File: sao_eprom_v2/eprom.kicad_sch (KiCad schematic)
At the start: 7 parts, among them U4 74LS573, U7 74LS573

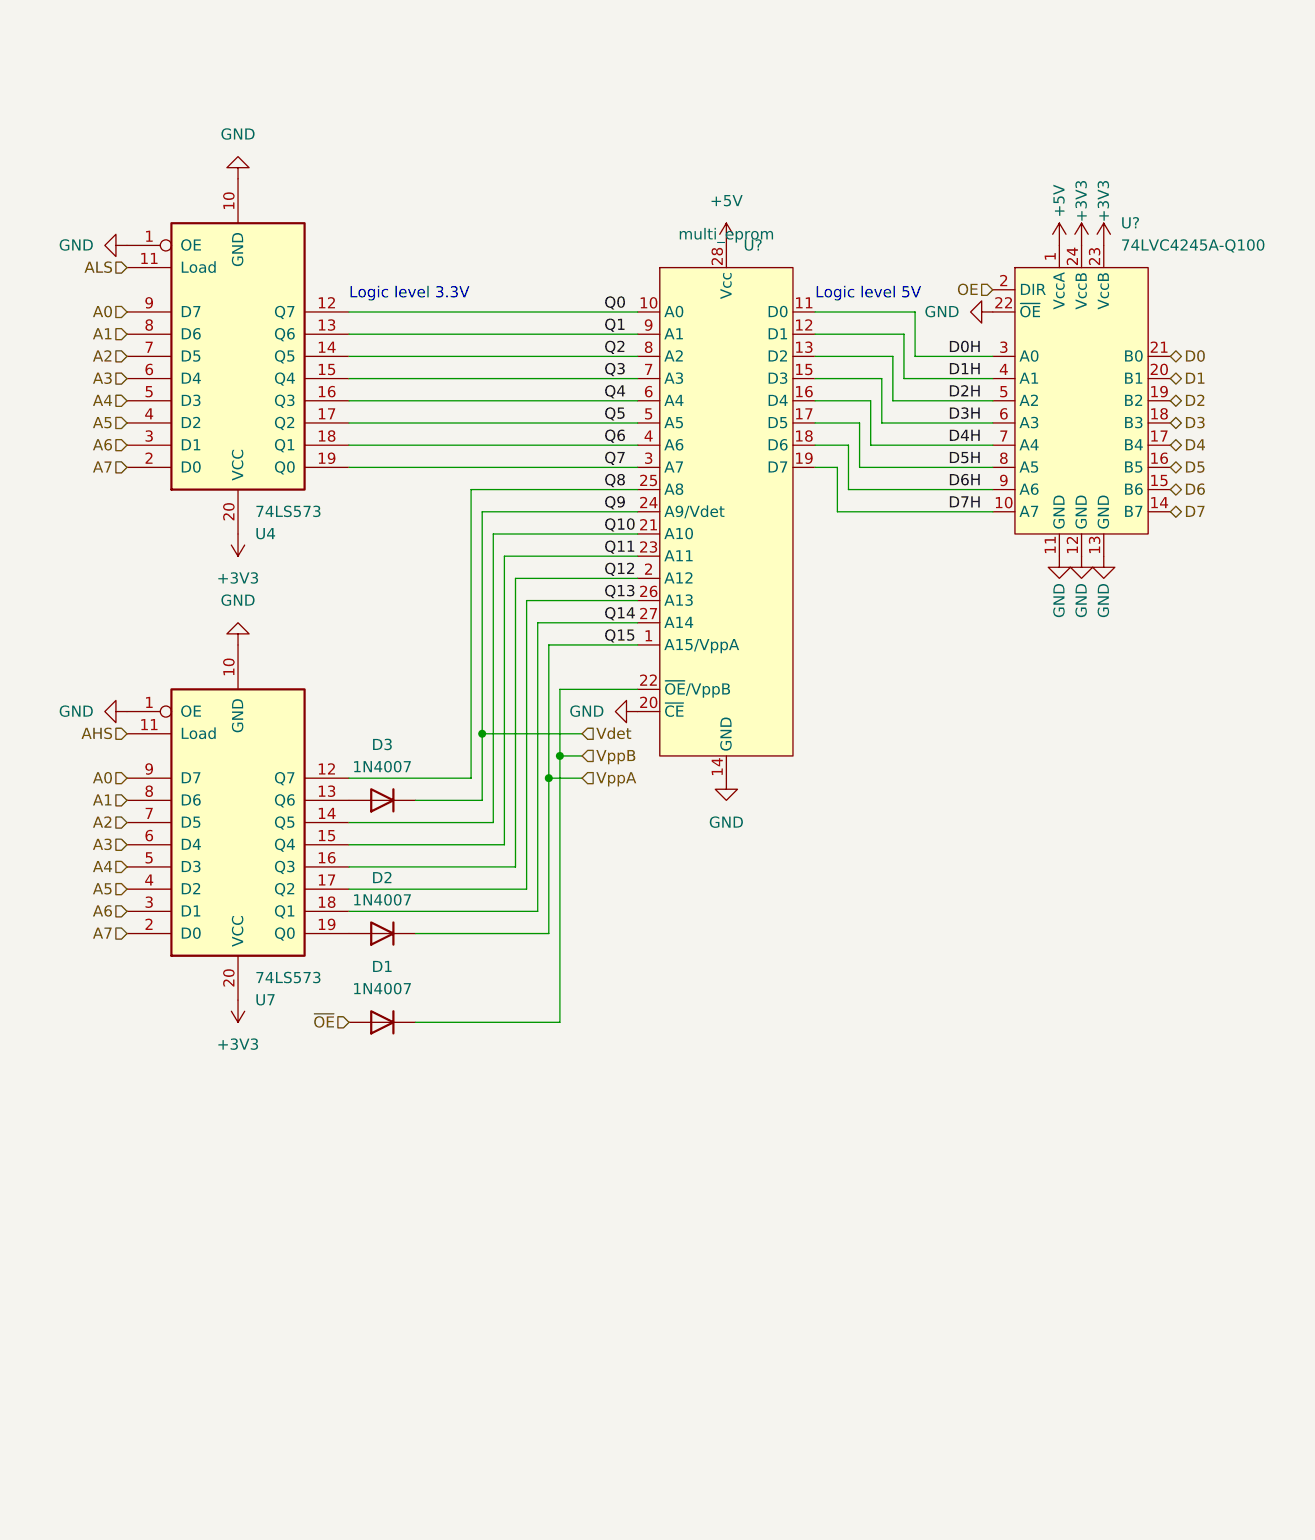
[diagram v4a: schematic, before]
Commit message: Add some blinkenlights!
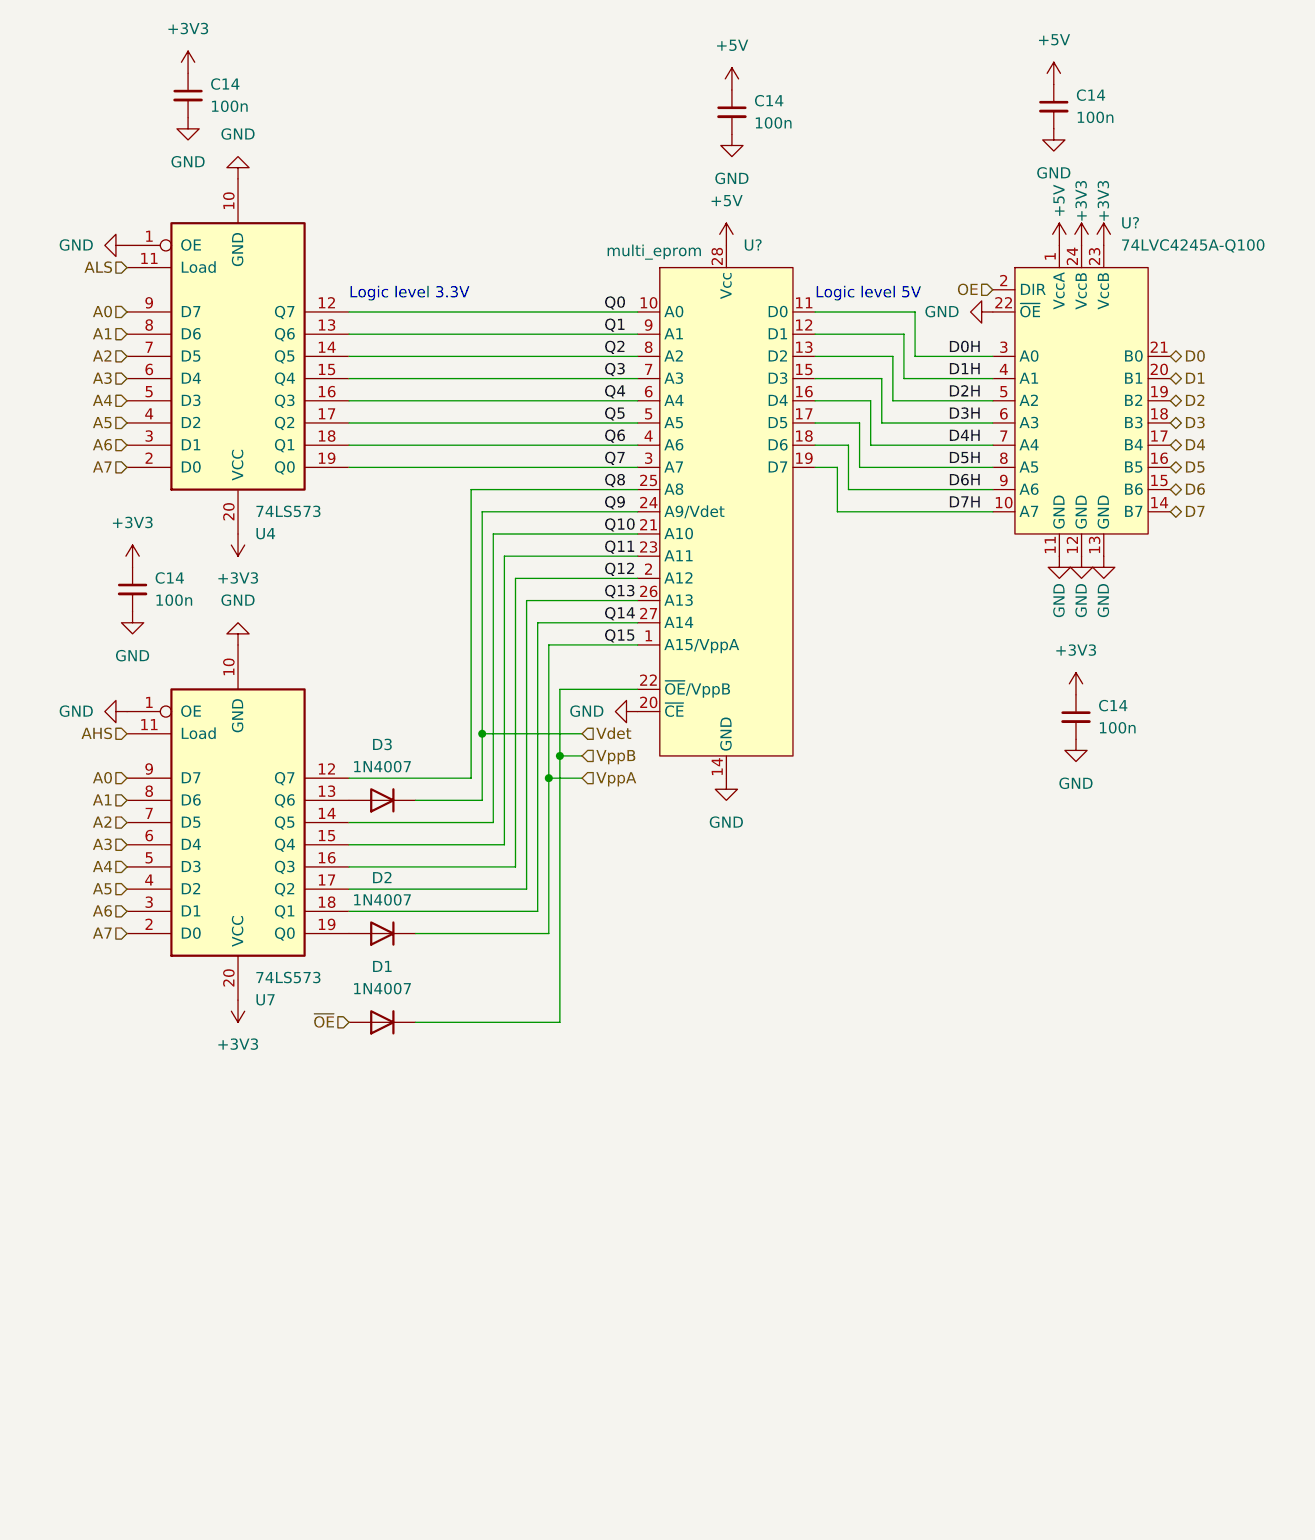
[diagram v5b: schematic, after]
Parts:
- added C14 (x5): 100n, Capacitor_SMD:C_0402_1005Metric_Pad0.74x0.62mm_HandSolder, symbol Device:C_Small
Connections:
- net +3V3: now also C14.1, C14.1, C14.1
- net +5V: now also C14.1, C14.1
- net GND: now also C14.2, C14.2, C14.2, C14.2, C14.2

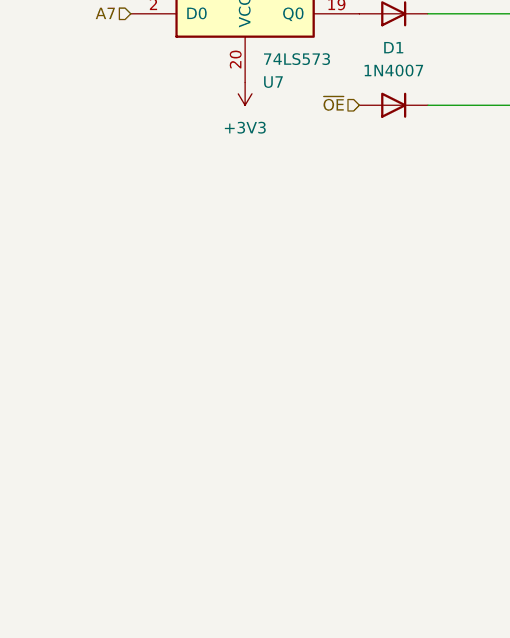
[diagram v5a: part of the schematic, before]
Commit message: Now with QWIIC and TestPads!
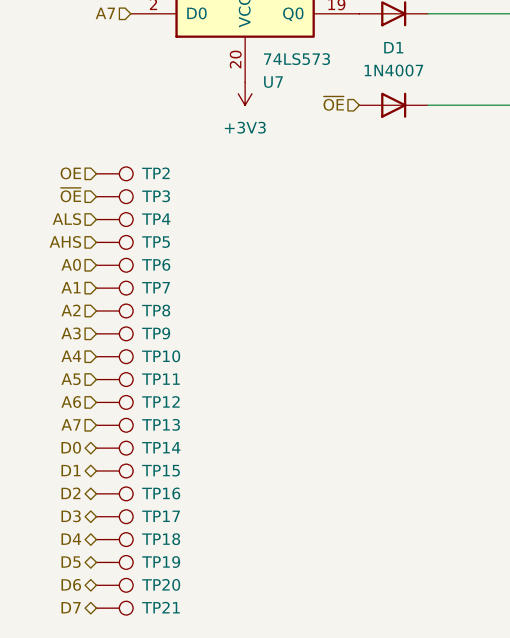
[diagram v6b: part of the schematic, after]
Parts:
- added TP10, TP11, TP12, TP13, TP14, TP15, TP16, TP17, TP18, TP19, TP2, TP20, TP21, TP3, TP4, TP5, TP6, TP7, TP8, TP9: TestPoint, TestPoint:TestPoint_Pad_D1.0mm, symbol Connector:TestPoint
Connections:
- net A0: now also TP6.1
- net A1: now also TP7.1
- net A2: now also TP8.1
- net A3: now also TP9.1
- net A4: now also TP10.1
- net A5: now also TP11.1
- net A6: now also TP12.1
- net A7: now also TP13.1
- net AHS: now also TP5.1
- net ALS: now also TP4.1
- net D0: now also TP14.1
- net D1: now also TP15.1
- net D2: now also TP16.1
- net D3: now also TP17.1
- net D4: now also TP18.1
- net D5: now also TP19.1
- net D6: now also TP20.1
- net D7: now also TP21.1
- net OE: now also TP2.1
- net ~{OE}: now also TP3.1

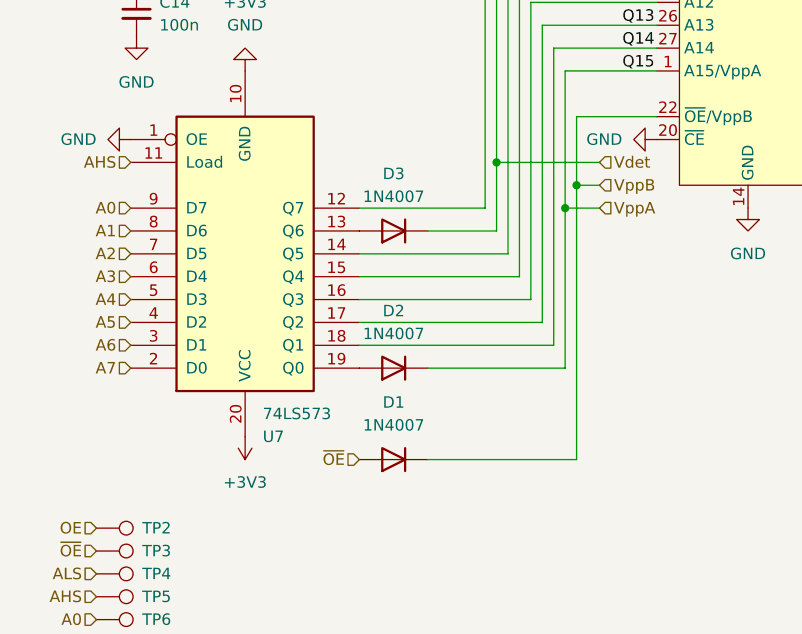
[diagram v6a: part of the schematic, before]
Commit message: Put yet another feedback in my design
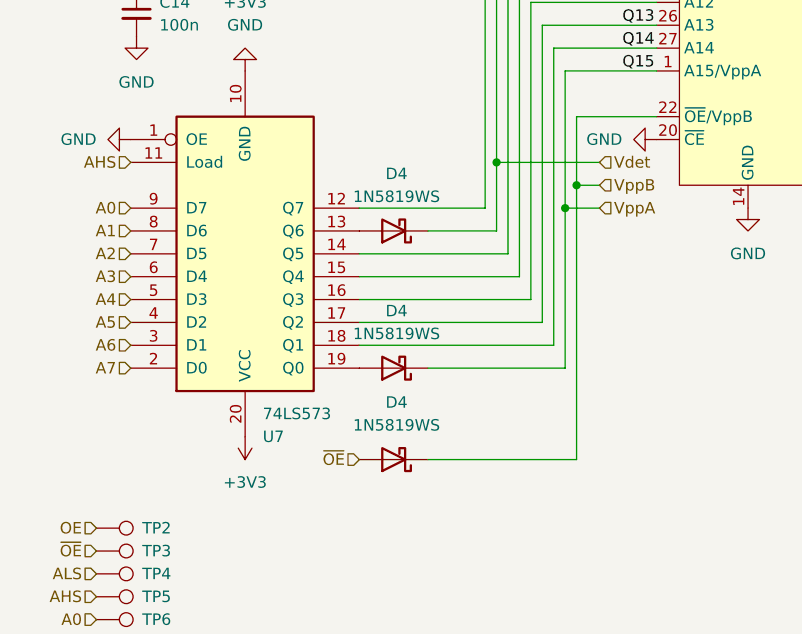
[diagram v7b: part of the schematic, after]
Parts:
- removed D1, D2, D3: 1N4007, Diode_SMD:D_SOD-123F, symbol Diode:1N4007
- added D4 (x3): 1N5819WS, Diode_SMD:D_SOD-323_HandSoldering, symbol Diode:1N5819WS
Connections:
- net Vdet: now also D4.1 (K)
- net VppA: now also D4.1 (K)
- net VppB: now also D4.1 (K)
- net ~{OE}: now also D4.2 (A)
- net at U7.13 (Q6): now also D4.2 (A)
- net at U7.19 (Q0): now also D4.2 (A)
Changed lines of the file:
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@@
-    )
-  )
-  (symbol (lib_id "Diode:1N4007") (at 87.63 101.6 180) (unit 1)
-    (in_bom yes) (on_board yes) (dnp no) (fields_autoplaced)
-    (property "Reference" "D3" (at 87.63 95.25 0)
-      (effects (font (size 1.27 1.27)))
-    )
-    (property "Value" "1N4007" (at 87.63 97.79 0)
-      (effects (font (size 1.27 1.27)))
-    )
-    (property "Footprint" "Diode_SMD:D_SOD-123F" (at 87.63 97.155 0)
-      (effects (font (size 1.27 1.27)) hide)
-    )
-    (property "Datasheet" "http://www.vishay.com/docs/88503/1n4001.pdf" (at 87.63 101.6 0)
-      (effects (font (size 1.27 1.27)) hide)
-    )
-    (property "Sim.Device" "D" (at 87.63 101.6 0)
-      (effects (font (size 1.27 1.27)) hide)
-    )
-    (property "Sim.Pins" "1=K 2=A" (at 87.63 101.6 0)
-      (effects (font (size 1.27 1.27)) hide)
-    )
-    (pin "1")
-    (pin "2")
-    (instances
-      (project "sao_eprom_v2"
-        (path "/07beccdd-32b3-4f03-aa51-fb5544b6f2d4/1053addf-4f12-44cd-9743-7d35ca2d08ac"
-          (reference "D3") (unit 1)
-        )
-      )
     )
   )
@@
     )
   )
-  (symbol (lib_id "Diode:1N4007") (at 87.63 127 180) (unit 1)
-    (in_bom yes) (on_board yes) (dnp no) (fields_autoplaced)
-    (property "Reference" "D1" (at 87.63 120.65 0)
-      (effects (font (size 1.27 1.27)))
-    )
-    (property "Value" "1N4007" (at 87.63 123.19 0)
-      (effects (font (size 1.27 1.27)))
-    )
-    (property "Footprint" "Diode_SMD:D_SOD-123F" (at 87.63 122.555 0)
-      (effects (font (size 1.27 1.27)) hide)
-    )
-    (property "Datasheet" "http://www.vishay.com/docs/88503/1n4001.pdf" (at 87.63 127 0)
-      (effects (font (size 1.27 1.27)) hide)
-    )
-    (property "Sim.Device" "D" (at 87.63 127 0)
-      (effects (font (size 1.27 1.27)) hide)
-    )
-    (property "Sim.Pins" "1=K 2=A" (at 87.63 127 0)
-      (effects (font (size 1.27 1.27)) hide)
-    )
-    (pin "1")
-    (pin "2")
-    (instances
-      (project "sao_eprom_v2"
-        (path "/07beccdd-32b3-4f03-aa51-fb5544b6f2d4/1053addf-4f12-44cd-9743-7d35ca2d08ac"
-          (reference "D1") (unit 1)
-        )
-      )
-    )
-  )
   (symbol (lib_id "power:GND") (at 116.84 91.44 270) (unit 1)
     (in_bom yes) (on_board yes) (dnp no) (fields_autoplaced)
@@
         (path "/07beccdd-32b3-4f03-aa51-fb5544b6f2d4/1053addf-4f12-44cd-9743-7d35ca2d08ac"
           (reference "C26") (unit 1)
-        )
-      )
-    )
-  )
-  (symbol (lib_id "Diode:1N4007") (at 87.63 116.84 180) (unit 1)
-    (in_bom yes) (on_board yes) (dnp no) (fields_autoplaced)
-    (property "Reference" "D2" (at 87.63 110.49 0)
-      (effects (font (size 1.27 1.27)))
-    )
-    (property "Value" "1N4007" (at 87.63 113.03 0)
-      (effects (font (size 1.27 1.27)))
-    )
-    (property "Footprint" "Diode_SMD:D_SOD-123F" (at 87.63 112.395 0)
-      (effects (font (size 1.27 1.27)) hide)
-    )
-    (property "Datasheet" "http://www.vishay.com/docs/88503/1n4001.pdf" (at 87.63 116.84 0)
-      (effects (font (size 1.27 1.27)) hide)
-    )
-    (property "Sim.Device" "D" (at 87.63 116.84 0)
-      (effects (font (size 1.27 1.27)) hide)
-    )
-    (property "Sim.Pins" "1=K 2=A" (at 87.63 116.84 0)
-      (effects (font (size 1.27 1.27)) hide)
-    )
-    (pin "1")
-    (pin "2")
-    (instances
-      (project "sao_eprom_v2"
-        (path "/07beccdd-32b3-4f03-aa51-fb5544b6f2d4/1053addf-4f12-44cd-9743-7d35ca2d08ac"
-          (reference "D2") (unit 1)
         )
       )
@@
     )
   )
+  (symbol (lib_id "Diode:1N5819WS") (at 87.63 101.6 180) (unit 1)
+    (in_bom yes) (on_board yes) (dnp no) (fields_autoplaced)
+    (property "Reference" "D4" (at 87.9475 95.25 0)
+      (effects (font (size 1.27 1.27)))
+    )
+    (property "Value" "1N5819WS" (at 87.9475 97.79 0)
+      (effects (font (size 1.27 1.27)))
+    )
+    (property "Footprint" "Diode_SMD:D_SOD-323_HandSoldering" (at 87.63 97.155 0)
+      (effects (font (size 1.27 1.27)) hide)
+    )
+    (property "Datasheet" "https://datasheet.lcsc.com/lcsc/2204281430_Guangdong-Hottech-1N5819WS_C191023.pdf" (at 87.63 101.6 0)
+      (effects (font (size 1.27 1.27)) hide)
+    )
+    (pin "1")
+    (pin "2")
+    (instances
+      (project "sao_eprom_v2"
+        (path "/07beccdd-32b3-4f03-aa51-fb5544b6f2d4/e608ecd4-0557-4bb4-9ac0-2ae7e9dd9344"
+          (reference "D4") (unit 1)
+        )
+        (path "/07beccdd-32b3-4f03-aa51-fb5544b6f2d4/1053addf-4f12-44cd-9743-7d35ca2d08ac"
+          (reference "D3") (unit 1)
+        )
+      )
+      (project "vfd"
+        (path "/c6c7f0b1-e719-4cc4-9f66-98fb677fcafc"
+          (reference "D1") (unit 1)
+        )
+      )
+    )
+  )
   (symbol (lib_id "Connector:TestPoint") (at 54.61 149.86 270) (unit 1)
     (in_bom yes) (on_board yes) (dnp no) (fields_autoplaced)
@@
     )
   )
+  (symbol (lib_id "Diode:1N5819WS") (at 87.63 127 180) (unit 1)
+    (in_bom yes) (on_board yes) (dnp no) (fields_autoplaced)
+    (property "Reference" "D4" (at 87.9475 120.65 0)
+      (effects (font (size 1.27 1.27)))
+    )
+    (property "Value" "1N5819WS" (at 87.9475 123.19 0)
+      (effects (font (size 1.27 1.27)))
+    )
+    (property "Footprint" "Diode_SMD:D_SOD-323_HandSoldering" (at 87.63 122.555 0)
+      (effects (font (size 1.27 1.27)) hide)
+    )
+    (property "Datasheet" "https://datasheet.lcsc.com/lcsc/2204281430_Guangdong-Hottech-1N5819WS_C191023.pdf" (at 87.63 127 0)
+      (effects (font (size 1.27 1.27)) hide)
+    )
+    (pin "1")
+    (pin "2")
+    (instances
+      (project "sao_eprom_v2"
+        (path "/07beccdd-32b3-4f03-aa51-fb5544b6f2d4/e608ecd4-0557-4bb4-9ac0-2ae7e9dd9344"
+          (reference "D4") (unit 1)
+        )
+        (path "/07beccdd-32b3-4f03-aa51-fb5544b6f2d4/1053addf-4f12-44cd-9743-7d35ca2d08ac"
+          (reference "D1") (unit 1)
+        )
+      )
+      (project "vfd"
+        (path "/c6c7f0b1-e719-4cc4-9f66-98fb677fcafc"
+          (reference "D1") (unit 1)
+        )
+      )
+    )
+  )
   (symbol (lib_id "power:GND") (at 58.42 38.1 270) (mirror x) (unit 1)
     (in_bom yes) (on_board yes) (dnp no) (fields_autoplaced)
@@
         )
       )
+    )
+  )
+  (symbol (lib_id "Diode:1N5819WS") (at 87.63 116.84 180) (unit 1)
+    (in_bom yes) (on_board yes) (dnp no) (fields_autoplaced)
+    (property "Reference" "D4" (at 87.9475 110.49 0)
+      (effects (font (size 1.27 1.27)))
+    )
+    (property "Value" "1N5819WS" (at 87.9475 113.03 0)
+      (effects (font (size 1.27 1.27)))
+    )
+    (property "Footprint" "Diode_SMD:D_SOD-323_HandSoldering" (at 87.63 112.395 0)
+      (effects (font (size 1.27 1.27)) hide)
+    )
+    (property "Datasheet" "https://datasheet.lcsc.com/lcsc/2204281430_Guangdong-Hottech-1N5819WS_C191023.pdf" (at 87.63 116.84 0)
+      (effects (font (size 1.27 1.27)) hide)
+    )
+    (pin "1")
+    (pin "2")
+    (instances
+      (project "sao_eprom_v2"
+        (path "/07beccdd-32b3-4f03-aa51-fb5544b6f2d4/e608ecd4-0557-4bb4-9ac0-2ae7e9dd9344"
+          (reference "D4") (unit 1)
+        )
+        (path "/07beccdd-32b3-4f03-aa51-fb5544b6f2d4/1053addf-4f12-44cd-9743-7d35ca2d08ac"
+          (reference "D2") (unit 1)
+        )
+      )
+      (project "vfd"
+        (path "/c6c7f0b1-e719-4cc4-9f66-98fb677fcafc"
+          (reference "D1") (unit 1)
+        )
+      )
